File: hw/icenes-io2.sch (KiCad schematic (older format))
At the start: 13 parts

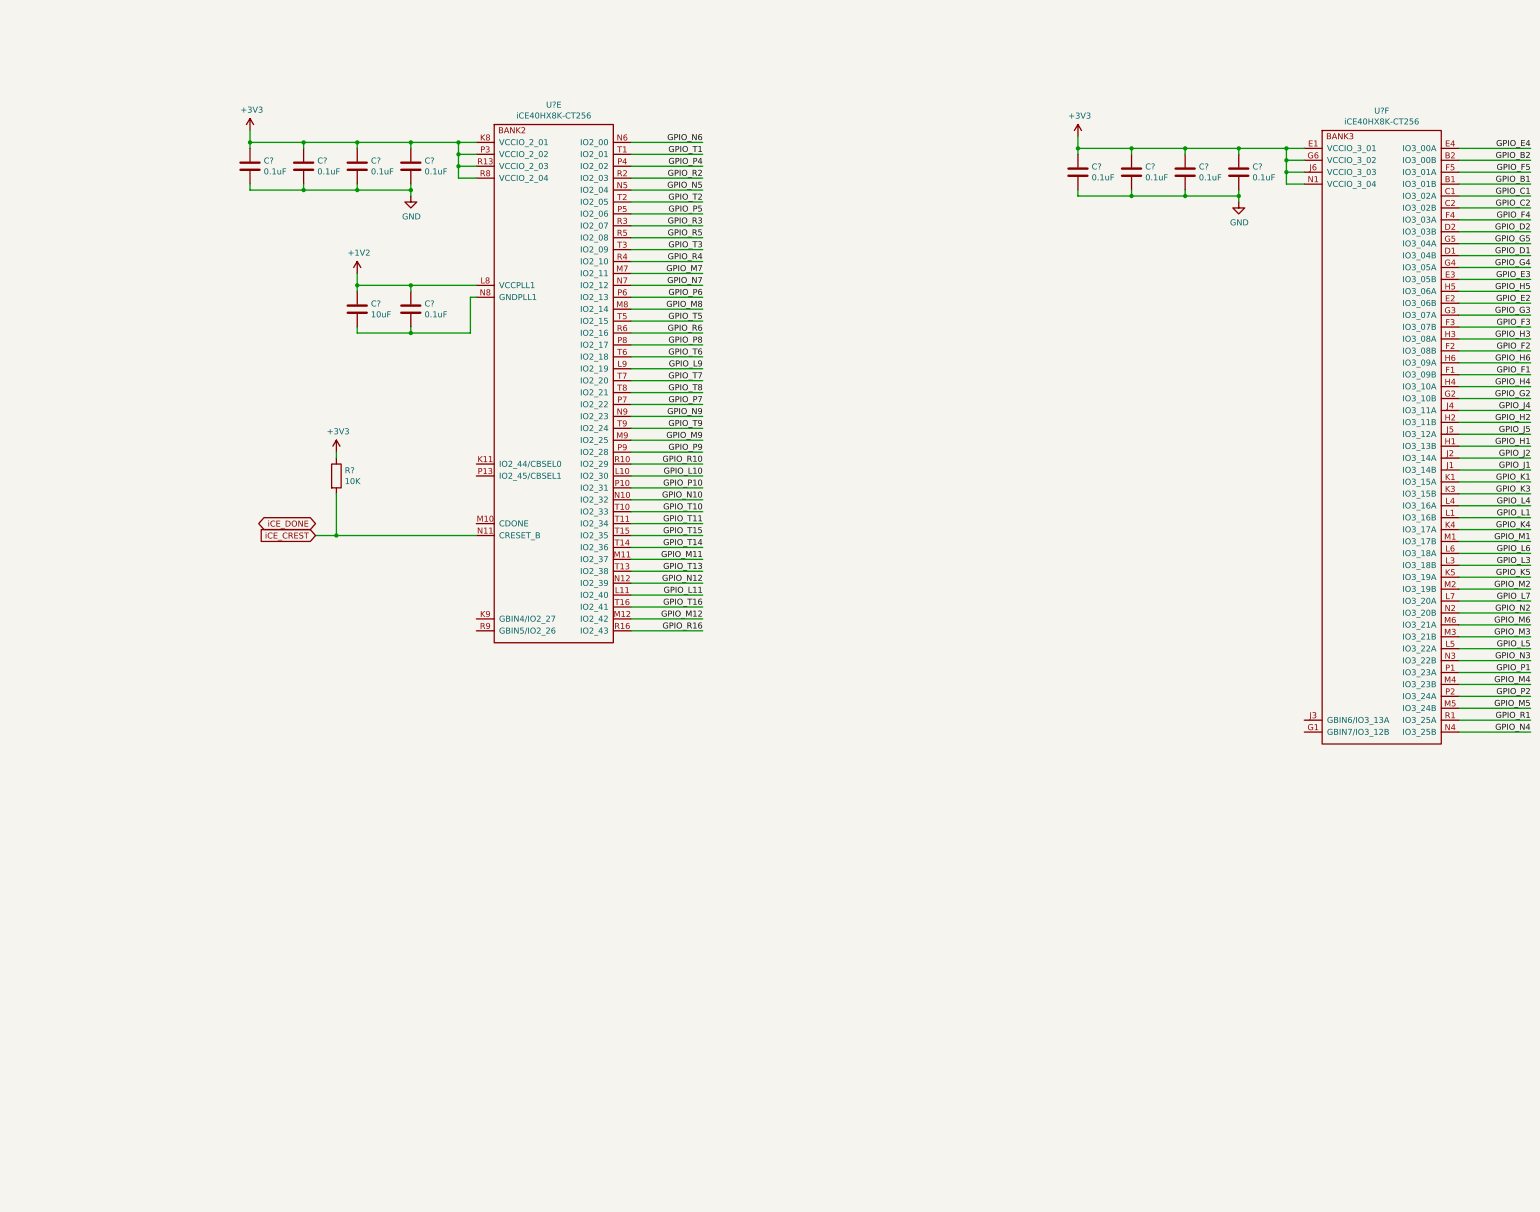
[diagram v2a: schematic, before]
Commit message: GPIO headers for banks 2 and 3.
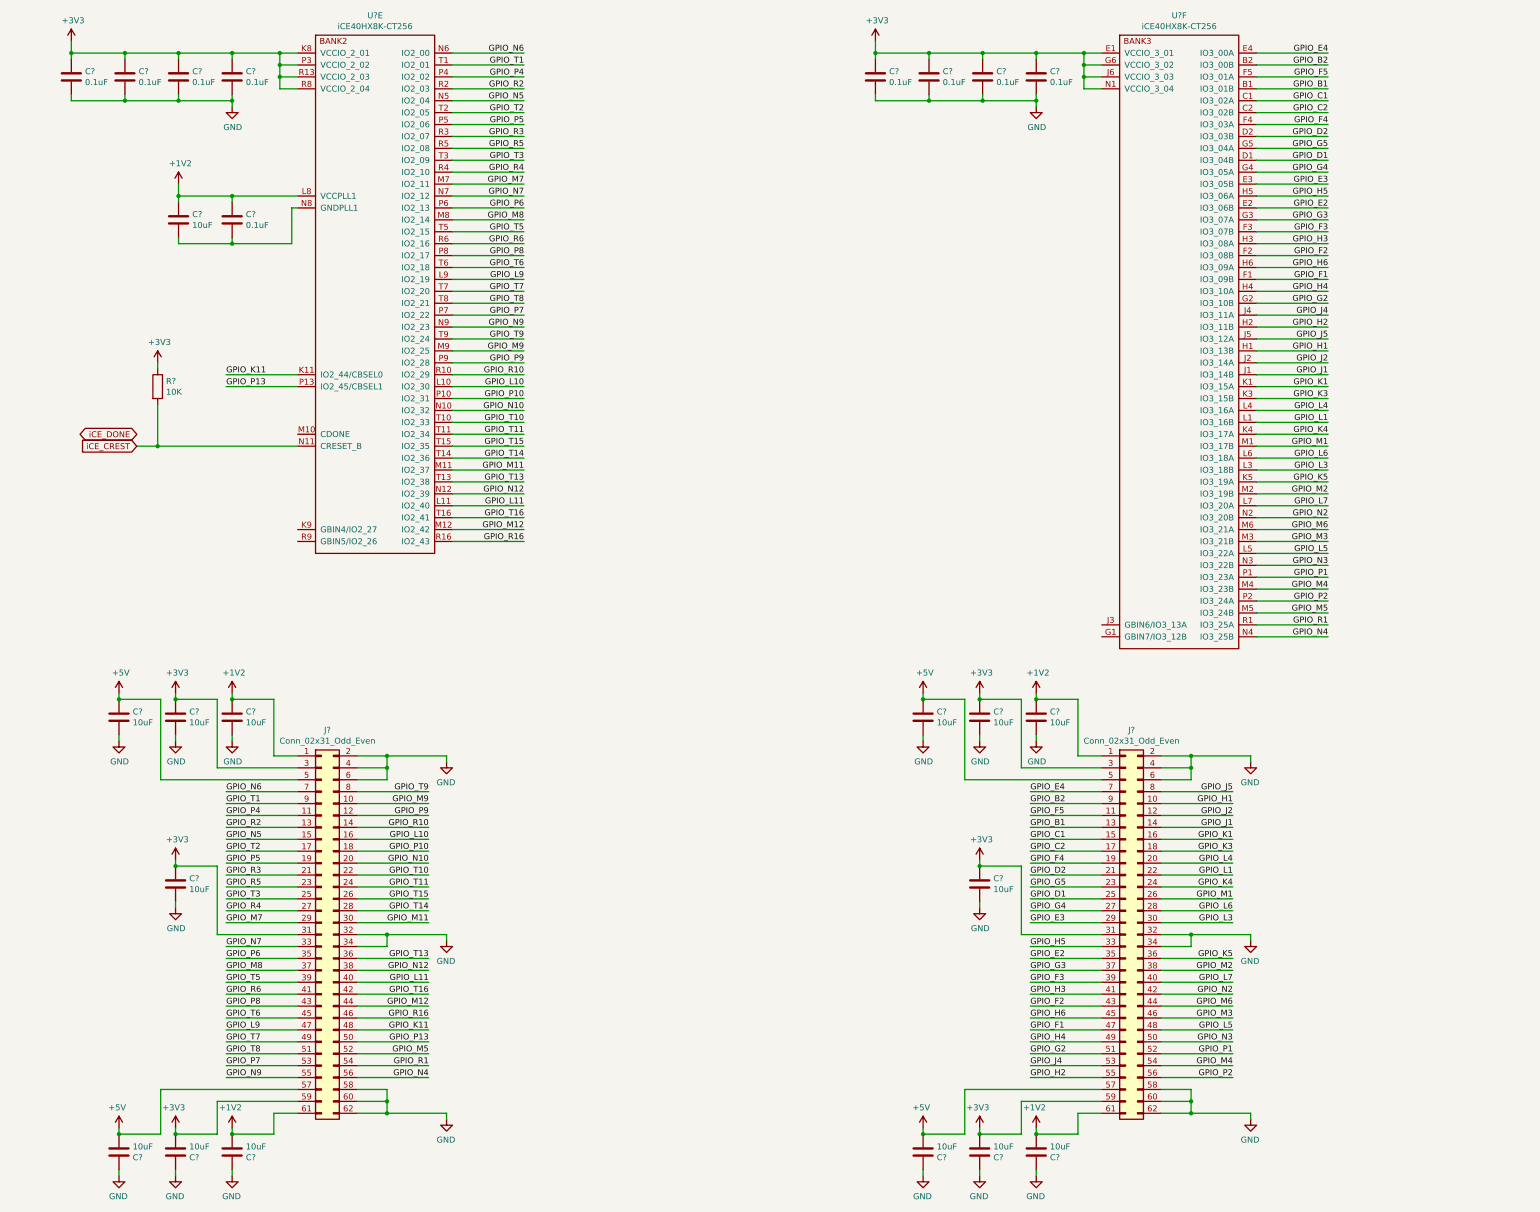
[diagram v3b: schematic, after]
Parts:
- added C? (x14): C10uF, Capacitor_SMD:C_0603_1608Metric_Pad1.05x0.95mm_HandSolder, symbol icenes-library:C10uF
- added J? (x2): Conn_02x31_Odd_Even, Connector_PinSocket_2.54mm:PinSocket_2x31_P2.54mm_Vertical, symbol icenes-library:Conn_02x31_Odd_Even
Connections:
- net +1V2: now also C?.1, C?.1, C?.2, C?.2, J?.1 (Pin_1), J?.1 (Pin_1), J?.61 (Pin_61), J?.61 (Pin_61)
- net +3V3: now also C?.1, C?.1, C?.1, C?.1, C?.2, C?.2, J?.3 (Pin_3), J?.3 (Pin_3), J?.31 (Pin_31), J?.31 (Pin_31), J?.59 (Pin_59), J?.59 (Pin_59)
- net GND: now also C?.1, C?.1, C?.1, C?.1, C?.1, C?.1, C?.2, C?.2, C?.2, C?.2, C?.2, C?.2, C?.2, C?.2, J?.2 (Pin_2), J?.2 (Pin_2), J?.32 (Pin_32), J?.32 (Pin_32), J?.34 (Pin_34), J?.34 (Pin_34), J?.4 (Pin_4), J?.4 (Pin_4), J?.58 (Pin_58), J?.58 (Pin_58), J?.6 (Pin_6), J?.6 (Pin_6), J?.60 (Pin_60), J?.60 (Pin_60), J?.62 (Pin_62), J?.62 (Pin_62)
- net GPIO_B1: now also J?.13 (Pin_13)
- net GPIO_B2: now also J?.9 (Pin_9)
- net GPIO_C1: now also J?.15 (Pin_15)
- net GPIO_C2: now also J?.17 (Pin_17)
- net GPIO_D1: now also J?.25 (Pin_25)
- net GPIO_D2: now also J?.21 (Pin_21)
- net GPIO_E2: now also J?.35 (Pin_35)
- net GPIO_E3: now also J?.29 (Pin_29)
- net GPIO_E4: now also J?.7 (Pin_7)
- net GPIO_F1: now also J?.47 (Pin_47)
- net GPIO_F2: now also J?.43 (Pin_43)
- net GPIO_F3: now also J?.39 (Pin_39)
- net GPIO_F4: now also J?.19 (Pin_19)
- net GPIO_F5: now also J?.11 (Pin_11)
- net GPIO_G2: now also J?.51 (Pin_51)
- net GPIO_G3: now also J?.37 (Pin_37)
- net GPIO_G4: now also J?.27 (Pin_27)
- net GPIO_G5: now also J?.23 (Pin_23)
- net GPIO_H1: now also J?.10 (Pin_10)
- net GPIO_H2: now also J?.55 (Pin_55)
- net GPIO_H3: now also J?.41 (Pin_41)
- net GPIO_H4: now also J?.49 (Pin_49)
- net GPIO_H5: now also J?.33 (Pin_33)
- net GPIO_H6: now also J?.45 (Pin_45)
- net GPIO_J1: now also J?.14 (Pin_14)
- net GPIO_J2: now also J?.12 (Pin_12)
- net GPIO_J4: now also J?.53 (Pin_53)
- net GPIO_J5: now also J?.8 (Pin_8)
- net GPIO_K1: now also J?.16 (Pin_16)
- net GPIO_K3: now also J?.18 (Pin_18)
- net GPIO_K4: now also J?.24 (Pin_24)
- net GPIO_K5: now also J?.36 (Pin_36)
- net GPIO_L1: now also J?.22 (Pin_22)
- net GPIO_L10: now also J?.16 (Pin_16)
- net GPIO_L11: now also J?.40 (Pin_40)
- net GPIO_L3: now also J?.30 (Pin_30)
- net GPIO_L4: now also J?.20 (Pin_20)
- net GPIO_L5: now also J?.48 (Pin_48)
- net GPIO_L6: now also J?.28 (Pin_28)
- net GPIO_L7: now also J?.40 (Pin_40)
- net GPIO_L9: now also J?.47 (Pin_47)
- net GPIO_M1: now also J?.26 (Pin_26)
- net GPIO_M11: now also J?.30 (Pin_30)
- net GPIO_M12: now also J?.44 (Pin_44)
- net GPIO_M2: now also J?.38 (Pin_38)
- net GPIO_M3: now also J?.46 (Pin_46)
- net GPIO_M4: now also J?.54 (Pin_54)
- net GPIO_M5: now also J?.52 (Pin_52)
- net GPIO_M6: now also J?.44 (Pin_44)
- net GPIO_M7: now also J?.29 (Pin_29)
- net GPIO_M8: now also J?.37 (Pin_37)
- net GPIO_M9: now also J?.10 (Pin_10)
- net GPIO_N10: now also J?.20 (Pin_20)
- net GPIO_N12: now also J?.38 (Pin_38)
- net GPIO_N2: now also J?.42 (Pin_42)
- net GPIO_N3: now also J?.50 (Pin_50)
- net GPIO_N4: now also J?.56 (Pin_56)
- net GPIO_N5: now also J?.15 (Pin_15)
- net GPIO_N6: now also J?.7 (Pin_7)
- net GPIO_N7: now also J?.33 (Pin_33)
- net GPIO_N9: now also J?.55 (Pin_55)
- net GPIO_P1: now also J?.52 (Pin_52)
- net GPIO_P10: now also J?.18 (Pin_18)
- net GPIO_P2: now also J?.56 (Pin_56)
- net GPIO_P4: now also J?.11 (Pin_11)
- net GPIO_P5: now also J?.19 (Pin_19)
- net GPIO_P6: now also J?.35 (Pin_35)
- net GPIO_P7: now also J?.53 (Pin_53)
- net GPIO_P8: now also J?.43 (Pin_43)
- net GPIO_P9: now also J?.12 (Pin_12)
- net GPIO_R1: now also J?.54 (Pin_54)
- net GPIO_R10: now also J?.14 (Pin_14)
- net GPIO_R16: now also J?.46 (Pin_46)
- net GPIO_R2: now also J?.13 (Pin_13)
- net GPIO_R3: now also J?.21 (Pin_21)
- net GPIO_R4: now also J?.27 (Pin_27)
- net GPIO_R5: now also J?.23 (Pin_23)
- net GPIO_R6: now also J?.41 (Pin_41)
- net GPIO_T1: now also J?.9 (Pin_9)
- net GPIO_T10: now also J?.22 (Pin_22)
- net GPIO_T11: now also J?.24 (Pin_24)
- net GPIO_T13: now also J?.36 (Pin_36)
- net GPIO_T14: now also J?.28 (Pin_28)
- net GPIO_T15: now also J?.26 (Pin_26)
- net GPIO_T16: now also J?.42 (Pin_42)
- net GPIO_T2: now also J?.17 (Pin_17)
- net GPIO_T3: now also J?.25 (Pin_25)
- net GPIO_T5: now also J?.39 (Pin_39)
- net GPIO_T6: now also J?.45 (Pin_45)
- net GPIO_T7: now also J?.49 (Pin_49)
- net GPIO_T8: now also J?.51 (Pin_51)
- net GPIO_T9: now also J?.8 (Pin_8)
- net GPIO_K11: now reaches U?.K11 (IO2_44/CBSEL0)
- net GPIO_K11: now also J?.48 (Pin_48)
- net GPIO_P13: now reaches U?.P13 (IO2_45/CBSEL1)
- net GPIO_P13: now also J?.50 (Pin_50)
- new net +5V: C?.1, C?.1, C?.2, C?.2, J?.5 (Pin_5), J?.5 (Pin_5), J?.57 (Pin_57), J?.57 (Pin_57)
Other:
- moved on the sheet: C?, R?, U?E, U?F

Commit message: Footprints.
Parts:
- U? (x2): Manufacturer (none) -> Lattice; Part number (none) -> iCE40HX8K-CT256
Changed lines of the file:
@@
 F 2 "Package_BGA:BGA-256_14.0x14.0mm_Layout16x16_P0.8mm_Ball0.45mm_Pad0.32mm_NSMD" H 3800 1200 50  0001 C CNN
 F 3 "" H 3800 1200 50  0001 C CNN
+F 4 "Lattice" H 3800 1200 50  0001 C CNN "Manufacturer"
+F 5 "iCE40HX8K-CT256" H 3800 1200 50  0001 C CNN "Part number"
 	5    3800 1200
 	1    0    0    -1
@@
 F 2 "Package_BGA:BGA-256_14.0x14.0mm_Layout16x16_P0.8mm_Ball0.45mm_Pad0.32mm_NSMD" H 10550 1200 50  0001 C CNN
 F 3 "" H 10550 1200 50  0001 C CNN
+F 4 "Lattice" H 10550 1200 50  0001 C CNN "Manufacturer"
+F 5 "iCE40HX8K-CT256" H 10550 1200 50  0001 C CNN "Part number"
 	6    10550 1200
 	1    0    0    -1

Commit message: Completed USB interface. Clock sources for PAL and NTSC frequencies. Added a 133MHz clock (max input to PLL). Some more stuff.
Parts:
- added C?: C0.1uF, Capacitor_SMD:C_0603_1608Metric_Pad1.05x0.95mm_HandSolder, symbol icenes-library:C0.1uF
- added D?: Green_LED, LED_SMD:LED_0805_2012Metric_Pad1.15x1.40mm_HandSolder, symbol icenes-library:Green_LED
- added R?: R_TBD, Resistor_SMD:R_0603_1608Metric_Pad1.05x0.95mm_HandSolder, symbol icenes-library:R_TBD
- added TP? (x3): TestPoint, TestPoint:TestPoint_Pad_D1.0mm, symbol icenes-library:TestPoint
- added X?: DSC1001BI2-133.0000T, icenes-library:MEMS_Microship_Ocillator_SMD_CDFN-4_5.0x3.2mm, symbol icenes-library:DSC1001BI2-133.0000T
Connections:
- net +3V3: now also C?.1, R?.1, X?.1 (STANDBY#), X?.4 (VDD)
- net GND: now also C?.2, D?.1 (K), X?.2 (GND)
- net iCE_CREST: now also TP?.1
- net iCE_DONE: now also U?.M10 (CDONE), D?.2 (A), R?.2, TP?.1
- net ICE_CLK_133MHz: now reaches U?.K9 (GBIN4/IO2_27)
- net ICE_CLK_133MHz: now also TP?.1, X?.3 (OUT)
- net ICE_CLK_12MHZ: now reaches U?.J3 (GBIN6/IO3_13A)
- no-connect marks 0 -> 2
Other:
- moved on the sheet: R?

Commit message: Minor fixes.
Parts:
- gave numbers to parts that had none: 35
